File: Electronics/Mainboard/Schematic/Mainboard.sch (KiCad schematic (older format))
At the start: 80 parts, among them J1 CONN_01X02, J10 CONN_01X04, J2 CONN_01X02, J3 CONN_01X02, J4 CONN_01X02, J5 CONN_01X02, J6 CONN_02X05, J7 CONN_02X20, J8 CONN_01X02, J9 CONN_01X02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

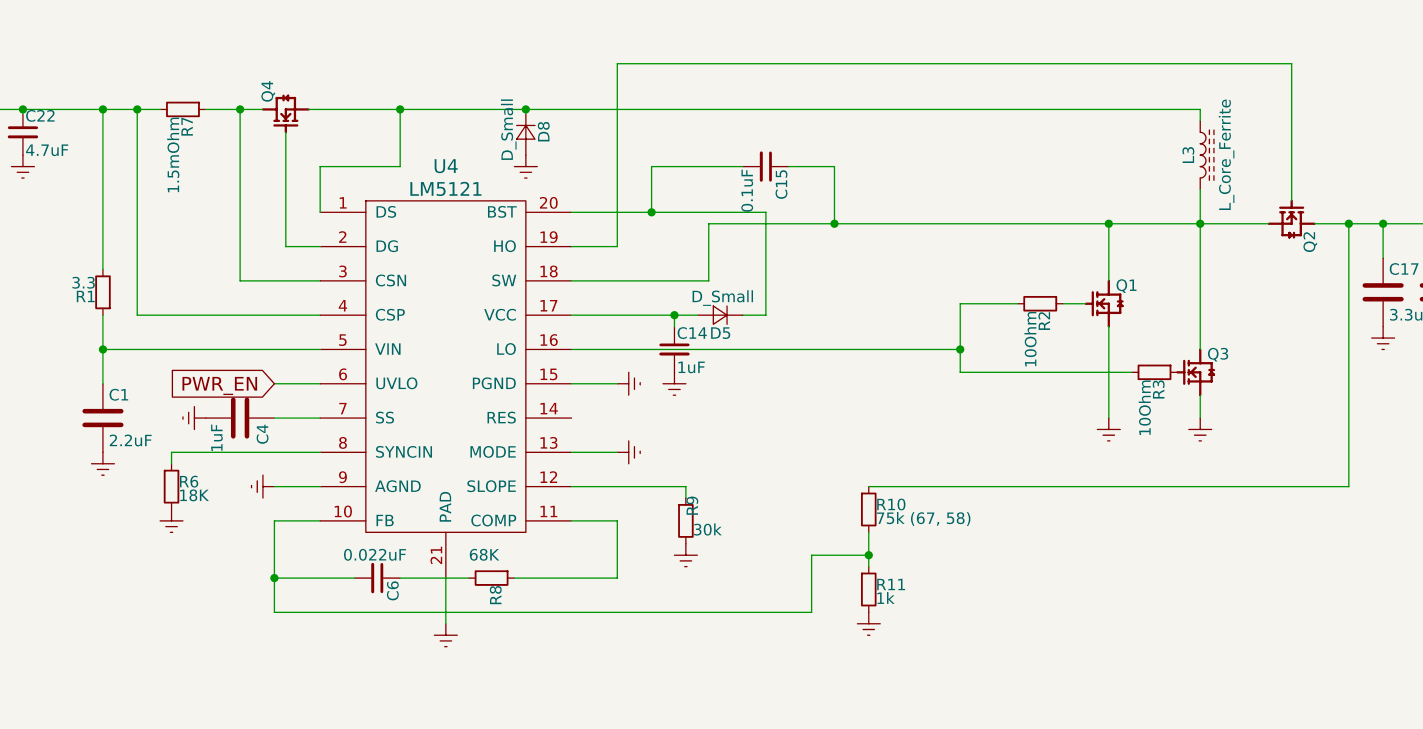
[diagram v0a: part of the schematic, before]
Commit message: Boost converter calculation
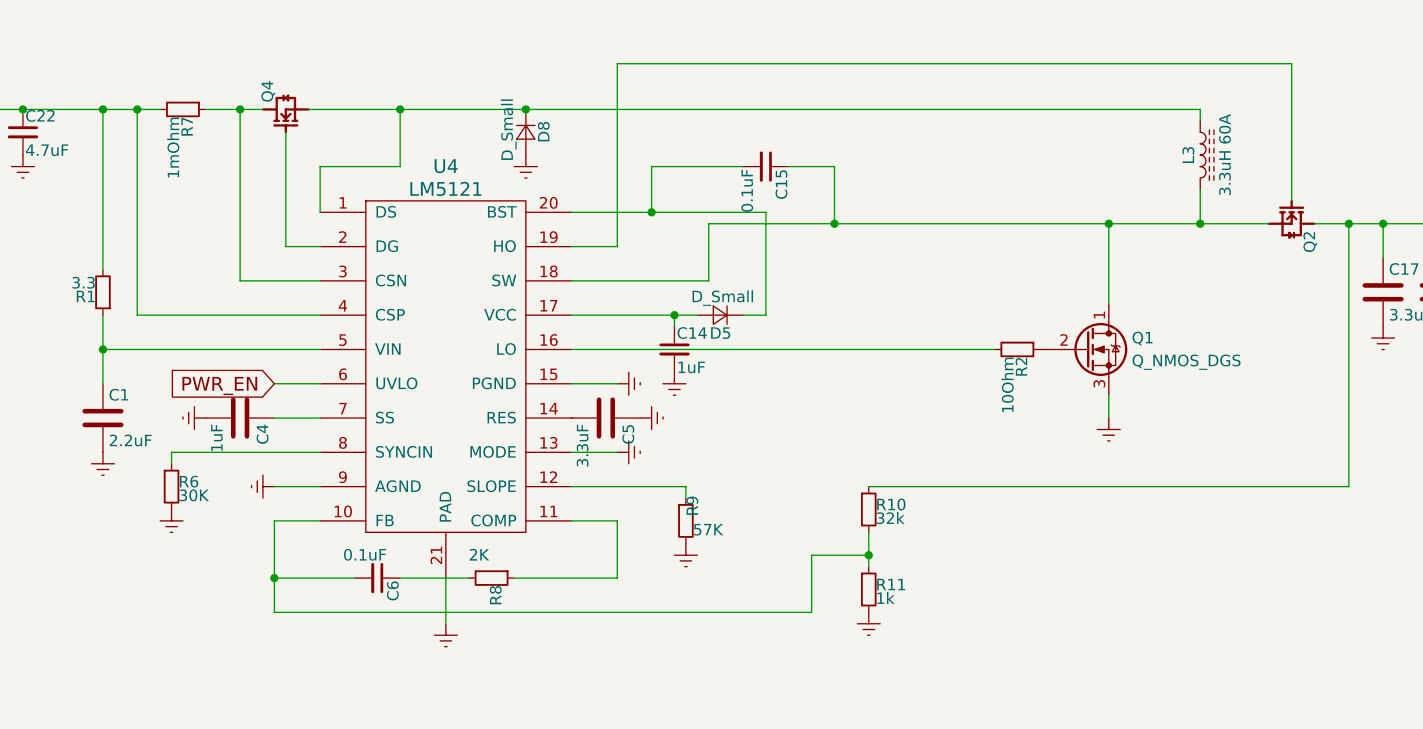
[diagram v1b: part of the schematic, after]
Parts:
- removed Q1, Q3: PSMN014-40YS, Dizzy:PSMN3R3-40YS, symbol PSMN014-40YS
- removed R3: 10Ohm, Resistors_SMD:R_0603, symbol R_Small
- added C5: 3.3uF, Capacitors_SMD:C_0603, symbol C
- added Q1: Q_NMOS_DGS, Dizzy:DirectFET-ME, symbol Q_NMOS_DGS
- C6: value 0.022uF -> 0.1uF
- L3: value L_Core_Ferrite -> 3.3uH 60A
- R10: value 75k (67, 58) -> 32k
- R6: value 18K -> 30K
- R7: value 1.5mOhm -> 1mOhm
- R8: value 68K -> 2K
- R9: value 30k -> 57K
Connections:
- net Earth: now also C5.1, Q1.3 (S)
- net at C15.1, L3.2, Q2.1 (S)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: now also Q1.1 (D)
- net at R2.1: now also Q1.2 (G)
- net at U4.14 (RES): now also C5.2
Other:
- moved on the sheet: R2

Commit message: started new mainboard
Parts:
- removed J7: CONN_02X20, Pin_Headers:Pin_Header_Straight_2x20_Pitch2.54mm, symbol CONN_02X20
- removed Q1: Q_NMOS_DGS, Dizzy:DirectFET-ME, symbol Q_NMOS_DGS
- added J11: M1, Dizzy:Hole-m3, symbol CONN_01X01
- added J12: M2, Dizzy:Hole-m3, symbol CONN_01X01
- added J13: M3, Dizzy:Hole-m3, symbol CONN_01X01
- added J14: M4, Dizzy:Hole-m3, symbol CONN_01X01
- added J7: CONN_02X10, Pin_Headers:Pin_Header_Straight_2x10_Pitch2.54mm_SMD, symbol CONN_02X10
- added Q1: BUK7Y7R8-80EX, Dizzy:PSMN3R3-40YS, symbol PSMN014-40YS
- added R3: 10Ohm, Resistors_SMD:R_0603, symbol R_Small
- J1, J2, J8, J9: footprint Pin_Headers:Pin_Header_Straight_1x02_Pitch2.54mm -> Dizzy:2x1.5-conn
- J10: footprint Pin_Headers:Pin_Header_Straight_1x04_Pitch2.54mm -> Dizzy:4x1.5-conn
- J3: footprint Dizzy:XT60 -> Dizzy:2x2.1-conn
- J4, J5: footprint Dizzy:xt30 -> Dizzy:2x2.1-conn
- L2: value 22uH -> 33uH
- Q2, Q4: value PSMN014-40YS -> BUK7Y7R8-80EX
- U2: value LM2678-5V -> LM2678-12V
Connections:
- net 3.3V: now also J7.10 (P10), J7.12 (P12), J7.14 (P14)
- net 5V: now also J7.15 (P15), J7.17 (P17), J7.19 (P19); no longer C13.1, C29.1, L2.2, U2.7 (FB)
- net CS: now also J7.7 (P7)
- net Earth: now also J7.4 (P4), J7.6 (P6), J7.8 (P8), Q1.1 (S), Q1.2 (S), Q1.3 (S)
- net MISO: now also J7.3 (P3)
- net MOSI: now also J7.1 (P1)
- net PWR_INT: now also J7.13 (P13)
- net RECVRDY: now also J7.11 (P11)
- net RESPRDY: now also J7.9 (P9)
- net SCK: now also J7.5 (P5)
- net ~PWR_KILL: now also J7.2 (P2)
- net at D8.1 (K), L3.1, Q4.1 (S)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: now also R14.2
- net at C15.1, L3.2, Q2.1 (S)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: now also Q1.5678 (D)
- net at C17.1, C18.1, Q2.5678 (D)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: no longer R14.2
- net at Q2.4 (G): now also R3.1; no longer U4.19 (HO)
- net at R2.1: now also Q1.4 (G)
- new net: R3.2, U4.19 (HO)
- new net 12V: C13.1, C29.1, J7.16 (P16), J7.18 (P18), J7.20 (P20), L2.2, U2.7 (FB)
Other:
- moved on the sheet: C27, J1, J2, J3, R14, R4, U10

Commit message: saving
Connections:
- net 12V: now also J9.2 (P2)
- net 5V: no longer J9.2 (P2)

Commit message: new mainboard
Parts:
- C22: value 4.7uF -> 20uF
- U8: value STM32F031G6U6 -> STM32F031K6U6
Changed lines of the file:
@@
 P 10800 3800
 F 0 "U8" H 10800 4250 60  0000 C CNN
-F 1 "STM32F031G6U6" H 10800 4350 60  0000 C CNN
+F 1 "STM32F031K6U6" H 10800 4350 60  0000 C CNN
 F 2 "Dizzy:UFQFPN32-small-pad" H 10800 3800 60  0001 C CNN
 F 3 "" H 10800 3800 60  0001 C CNN
@@
 P 900 1150
 F 0 "C22" H 910 1220 50  0000 L CNN
-F 1 "4.7uF" H 910 1070 50  0000 L CNN
+F 1 "20uF" H 910 1070 50  0000 L CNN
 F 2 "Capacitors_SMD:C_1812" H 900 1150 50  0001 C CNN
 F 3 "" H 900 1150 50  0001 C CNN

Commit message: body V2
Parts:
- removed C1: 2.2uF, Capacitors_SMD:C_0603, symbol C
- removed C14: 1uF, Capacitors_SMD:C_0603, symbol C_Small
- removed C15: 0.1uF, Capacitors_SMD:C_0805, symbol C_Small
- removed C17, C18: 3.3uF, Capacitors_SMD:C_1812, symbol C
- removed C4: 1uF, Capacitors_SMD:C_0603, symbol C
- removed C5: 3.3uF, Capacitors_SMD:C_0603, symbol C
- removed C6: 0.1uF, Capacitors_SMD:C_0603, symbol C_Small
- removed L3: 3.3uH 60A, Dizzy:PQ3218‐3R3‐70‐T, symbol L_Core_Ferrite
- removed Q1, Q2, Q4: BUK7Y7R8-80EX, Dizzy:PSMN3R3-40YS, symbol PSMN014-40YS
- removed R10: 32k, Resistors_SMD:R_0603, symbol R_Small
- removed R11: 1k, Resistors_SMD:R_0603, symbol R_Small
- removed R2, R3: 10Ohm, Resistors_SMD:R_0603, symbol R_Small
- removed R6: 30K, Resistors_SMD:R_0603, symbol R_Small
- removed R7: 1mOhm, Resistors_SMD:R_2512, symbol R_Small
- removed R8: 2K, Resistors_SMD:R_0603, symbol R_Small
- removed R9: 57K, Resistors_SMD:R_0603, symbol R_Small
- removed U4: LM5121, Housings_SSOP:HTSSOP-20-1EP_4.4x6.5mm_Pitch0.65mm_ThermalPad, symbol LM5121
- added J15, J16, J17, J18, J21, J22, J23, J24, J25, J26, J27: CONN_01X01, Dizzy:0.6x1-conn, symbol CONN_01X01
- added Q1: BSS123W, TO_SOT_Packages_SMD:SOT-323_SC-70, symbol Q_NMOS_GSD
- added Q2: SQJ459EP, Dizzy:SQJ459EP, symbol Q_PMOS_SGD
- added U3: ZXTR2012Z, TO_SOT_Packages_SMD:SOT-89-3, symbol ZXTR2012Z
- D5: footprint Diodes_SMD:D_SOD-323 -> Diodes_SMD:D_SMA
- R1: value 3.3 -> 1K
- U10: value LTC2954 -> LTC2954-1
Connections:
- net +90V: now also D5.1 (K), D8.1 (K)
- net +BATT: now also R14.2, Q2.1 (S), U3.2 (IN); no longer U10.4 (VIN)
- net CS: now also J27.1 (P1)
- net Earth: now also D5.2 (A), Q1.2 (S), U3.1 (GND)
- net I_ADC: now also J15.1 (P1)
- net MISO: now also J25.1 (P1)
- net MOSI: now also J26.1 (P1)
- net PWR_EN: now also J23.1 (P1), Q1.1 (G)
- net RECVRDY: now also J18.1 (P1)
- net RESPRDY: now also J17.1 (P1)
- net SCK: now also J24.1 (P1)
- net SCL: now also J22.1 (P1)
- net SDA: now also J21.1 (P1)
- net V_ADC: now also J16.1 (P1)
- net at U6.5 (I+): now also Q2.3 (D)
- net at R1.1: now also Q1.3 (D), Q2.2 (G)
- new net: U10.4 (VIN), U3.3 (OUT)
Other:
- moved on the sheet: C19, C21, R13, R14, R17, R18, U6

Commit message: saving
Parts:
- added R?: 50K ???, Resistors_SMD:R_0603, symbol R_Small
- C22: value 20uF -> 20uF 50V
- R1: value 1K -> 30K
- R14: value 62k 1% -> 30K 1%
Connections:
- net at Q2.2 (G), R1.1: now also R?.2; no longer Q1.3 (D)
- new net: Q1.3 (D), R?.1
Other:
- moved on the sheet: Q1
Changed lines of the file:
@@
 P 1600 1050
 F 0 "R14" H 1630 1070 50  0000 L CNN
-F 1 "62k 1%" H 1630 1010 50  0000 L CNN
+F 1 "30K 1%" H 1630 1010 50  0000 L CNN
 F 2 "Resistors_SMD:R_0603" H 1600 1050 50  0001 C CNN
 F 3 "" H 1600 1050 50  0001 C CNN
@@
 P 900 1150
 F 0 "C22" H 910 1220 50  0000 L CNN
-F 1 "20uF" H 910 1070 50  0000 L CNN
+F 1 "20uF 50V" H 910 1070 50  0000 L CNN
 F 2 "Capacitors_SMD:C_1812" H 900 1150 50  0001 C CNN
 F 3 "" H 900 1150 50  0001 C CNN
@@
 P 1350 1850
 F 0 "R1" H 1380 1870 50  0000 L CNN
-F 1 "1K" H 1380 1810 50  0000 L CNN
+F 1 "30K" H 1380 1810 50  0000 L CNN
 F 2 "Resistors_SMD:R_0603" H 1350 1850 50  0001 C CNN
 F 3 "" H 1350 1850 50  0001 C CNN
@@
 Connection ~ 1250 1850
 Wire Wire Line
-	1450 1850 1900 1850
+	1450 1850 2050 1850
 Connection ~ 1900 1850
-Text GLabel 2200 1600 2    60   Input ~ 0
+Text GLabel 2800 1600 2    60   Input ~ 0
 PWR_EN
 Wire Wire Line
@@
 L Earth #PWR057
 U 1 1 5D216C32
-P 1900 1400
-F 0 "#PWR057" H 1900 1150 50  0001 C CNN
-F 1 "Earth" H 1900 1250 50  0001 C CNN
-F 2 "" H 1900 1400 50  0001 C CNN
-F 3 "" H 1900 1400 50  0001 C CNN
-	1    1900 1400
+P 2500 1400
+F 0 "#PWR057" H 2500 1150 50  0001 C CNN
+F 1 "Earth" H 2500 1250 50  0001 C CNN
+F 2 "" H 2500 1400 50  0001 C CNN
+F 3 "" H 2500 1400 50  0001 C CNN
+	1    2500 1400
 	-1   0    0    1
 $EndComp
-Wire Wire Line
-	1900 1800 1900 1900
 $Comp
 L Q_NMOS_GSD Q1
 U 1 1 5D23F92A
-P 2000 1600
-F 0 "Q1" H 2200 1650 50  0000 L CNN
-F 1 "BSS123W" H 2200 1550 50  0000 L CNN
-F 2 "TO_SOT_Packages_SMD:SOT-323_SC-70" H 2200 1700 50  0001 C CNN
-F 3 "" H 2000 1600 50  0001 C CNN
-	1    2000 1600
+P 2600 1600
+F 0 "Q1" H 2800 1650 50  0000 L CNN
+F 1 "BSS123W" H 2800 1550 50  0000 L CNN
+F 2 "TO_SOT_Packages_SMD:SOT-323_SC-70" H 2800 1700 50  0001 C CNN
+F 3 "" H 2600 1600 50  0001 C CNN
+	1    2600 1600
 	-1   0    0    1
 $EndComp
 Text GLabel 15400 6450 0    60   Input ~ 0
 CS
+Wire Wire Line
+	1900 1850 1900 1900
+$Comp
+L R_Small R?
+U 1 1 5D3AEFD4
+P 2150 1850
+F 0 "R?" H 2180 1870 50  0000 L CNN
+F 1 "50K ???" H 2180 1810 50  0000 L CNN
+F 2 "Resistors_SMD:R_0603" H 2150 1850 50  0001 C CNN
+F 3 "" H 2150 1850 50  0001 C CNN
+	1    2150 1850
+	0    1    1    0
+$EndComp
+Wire Wire Line
+	2250 1850 2500 1850
+Wire Wire Line
+	2500 1850 2500 1800
 $EndSCHEMATC

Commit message: donno what I'm committing
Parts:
- removed C7, C8: 0.01uF 50V, Capacitors_SMD:C_0603, symbol C_Small
- removed D8: D_Small, Diodes_SMD:D_SMA, symbol D_Small
- removed Q1: BSS123W, TO_SOT_Packages_SMD:SOT-323_SC-70, symbol Q_NMOS_GSD
- removed Q2: SQJ459EP, Dizzy:SQJ459EP, symbol Q_PMOS_SGD
- removed U1: LM2678-3.3V, Dizzy:14-VSON, symbol LM2678
- removed U2: LM2678-12V, Dizzy:14-VSON, symbol LM2678
- added C1, C4, C5: 20uF 50V, Capacitors_SMD:C_1210, symbol C_Small
- added Q1: SQM120P04-04L, TO_SOT_Packages_SMD:TO-263-2, symbol Q_PMOS_GDS
- added U1: AP1501A-3.3V, TO_SOT_Packages_SMD:TO-263-5_TabPin3, symbol AP1501A
- added U2: AP1501A-12V, TO_SOT_Packages_SMD:TO-263-5_TabPin3, symbol AP1501A
- C22: footprint Capacitors_SMD:C_1812 -> Capacitors_SMD:C_1210
- D5: footprint Diodes_SMD:D_SMA -> Diodes_SMD:D_SMC
- R1: value 30K -> 47K
- R2: renamed from R?; value 50K ??? -> 47K
- U10: value LTC2954-1 -> LTC2954-2
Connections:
- net +90V: now also C4.1, C5.1
- net +BATT: now also C1.1, Q1.3 (S)
- net 12V: now also U2.4 (FB)
- net 3.3V: now also U1.4 (FB)
- net Earth: now also C10.2, C2.2, C3.2, C9.2, C1.2, C4.2, C5.2, U1.3 (GND), U2.3 (GND); no longer C10.1, C2.1, C3.1, C9.1
- net PWR_EN: now also R1.1, R2.2, U1.5 (SD), U2.5 (SD)
- net at D2.1 (K), L2.1: now also U2.2 (OUT)
- net at D1.1 (K), L1.1: now also U1.2 (OUT)
- net at U6.5 (I+): now also Q1.2 (D)
- net at R2.1: now also Q1.1 (G)
- new net: C3.1, C9.1, D3.1 (K), U2.1 (Vin)
- new net: C10.1, C2.1, D4.1 (K), U1.1 (Vin)
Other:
- moved on the sheet: C10, C2, C3, C9, R1, R2
